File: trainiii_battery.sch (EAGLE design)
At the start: 3 parts, among them J1 B3B-XH-A(LF)(SN), J2 B3B-XH-A(LF)(SN)

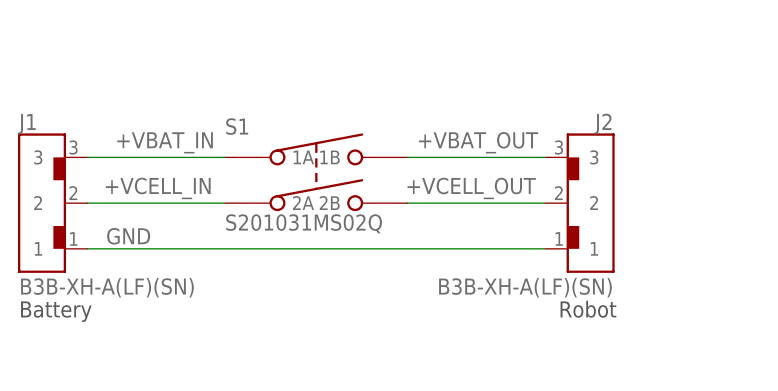
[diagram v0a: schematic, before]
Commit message: Added status LED, cleaned up board layout
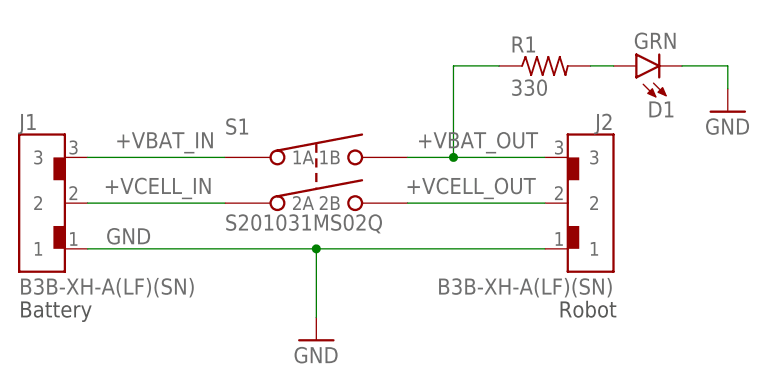
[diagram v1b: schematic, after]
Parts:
- added D1: GRN, SparkFun-LED:LED0603
- added R1: 330, rcl:R-US_R0603
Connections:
- new net LED_IN: D1.A, R1.2
- net +VBAT_OUT: now also R1.1
- net GND: now also D1.C

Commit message: Final Order v1.0
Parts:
- R1: value 330 -> 510
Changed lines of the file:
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@@
 <part name="S1" library="Trainiii Battery" deviceset="S201031MS02Q" device=""/>
 <part name="J2" library="Trainiii Battery" deviceset="B3B-XH-A(LF)(SN)" device=""/>
-<part name="R1" library="rcl" library_urn="urn:adsk.eagle:library:334" deviceset="R-US_" device="R0603" package3d_urn="urn:adsk.eagle:package:23555/3" value="330"/>
+<part name="R1" library="rcl" library_urn="urn:adsk.eagle:library:334" deviceset="R-US_" device="R0603" package3d_urn="urn:adsk.eagle:package:23555/3" value="510"/>
 <part name="GND1" library="supply1" library_urn="urn:adsk.eagle:library:371" deviceset="GND" device=""/>
 <part name="GND2" library="supply1" library_urn="urn:adsk.eagle:library:371" deviceset="GND" device=""/>
@@
 <sheet>
 <plain>
-<text x="38.1" y="50.8" size="1.778" layer="97">Battery</text>
-<text x="98.044" y="50.8" size="1.778" layer="97">Robot</text>
+<text x="38.1" y="50.8" size="1.778" layer="97" font="vector">Battery</text>
+<text x="98.044" y="50.8" size="1.778" layer="97" font="vector">Robot</text>
 </plain>
 <instances>
 <instance part="J1" gate="G$1" x="40.64" y="63.5" smashed="yes">
-<attribute name="NAME" x="38.1" y="71.628" size="1.778" layer="95"/>
-<attribute name="VALUE" x="38.1" y="53.34" size="1.778" layer="96"/>
+<attribute name="NAME" x="38.1" y="71.628" size="1.778" layer="95" font="vector"/>
+<attribute name="VALUE" x="38.1" y="53.34" size="1.778" layer="96" font="vector"/>
 </instance>
 <instance part="S1" gate="G$1" x="71.12" y="66.04" smashed="yes">
-<attribute name="NAME" x="60.96" y="71.12" size="1.778" layer="95"/>
-<attribute name="VALUE" x="60.96" y="60.452" size="1.778" layer="96"/>
+<attribute name="NAME" x="60.96" y="71.12" size="1.778" layer="95" font="vector"/>
+<attribute name="VALUE" x="60.96" y="60.452" size="1.778" layer="96" font="vector"/>
 </instance>
 <instance part="J2" gate="G$1" x="101.6" y="63.5" smashed="yes" rot="MR0">
-<attribute name="NAME" x="104.14" y="71.628" size="1.778" layer="95" rot="MR0"/>
-<attribute name="VALUE" x="104.14" y="53.34" size="1.778" layer="96" rot="MR0"/>
+<attribute name="NAME" x="104.14" y="71.628" size="1.778" layer="95" font="vector" rot="MR0"/>
+<attribute name="VALUE" x="104.14" y="53.34" size="1.778" layer="96" font="vector" rot="MR0"/>
 </instance>
 <instance part="R1" gate="G$1" x="96.52" y="78.74" smashed="yes">
-<attribute name="NAME" x="92.71" y="80.2386" size="1.778" layer="95"/>
-<attribute name="VALUE" x="92.71" y="75.438" size="1.778" layer="96"/>
+<attribute name="NAME" x="92.71" y="80.2386" size="1.778" layer="95" font="vector"/>
+<attribute name="VALUE" x="92.71" y="75.438" size="1.778" layer="96" font="vector"/>
 </instance>
 <instance part="GND1" gate="1" x="71.12" y="48.26" smashed="yes">
@@
 </instance>
 <instance part="GND2" gate="1" x="116.84" y="73.66" smashed="yes">
-<attribute name="VALUE" x="114.3" y="71.12" size="1.778" layer="96"/>
+<attribute name="VALUE" x="114.3" y="71.12" size="1.778" layer="96" font="vector"/>
 </instance>
 <instance part="D1" gate="G$1" x="106.68" y="78.74" smashed="yes" rot="R90">
-<attribute name="NAME" x="110.998" y="74.803" size="1.778" layer="95" rot="R180"/>
-<attribute name="VALUE" x="111.252" y="80.645" size="1.778" layer="96" rot="R180" align="top-left"/>
+<attribute name="NAME" x="110.998" y="74.803" size="1.778" layer="95" font="vector" rot="R180"/>
+<attribute name="VALUE" x="111.252" y="83.185" size="1.778" layer="96" font="vector" rot="R180"/>
 </instance>
 </instances>
@@
 <pinref part="J1" gate="G$1" pin="3"/>
 <wire x1="60.96" y1="68.58" x2="45.72" y2="68.58" width="0.1524" layer="91"/>
-<label x="48.768" y="69.596" size="1.778" layer="95"/>
+<label x="48.768" y="69.596" size="1.778" layer="95" font="vector"/>
 </segment>
 </net>
@@
 <pinref part="J1" gate="G$1" pin="2"/>
 <wire x1="60.96" y1="63.5" x2="45.72" y2="63.5" width="0.1524" layer="91"/>
-<label x="47.498" y="64.516" size="1.778" layer="95"/>
+<label x="47.498" y="64.516" size="1.778" layer="95" font="vector"/>
 </segment>
 </net>
@@
 <wire x1="81.28" y1="68.58" x2="86.36" y2="68.58" width="0.1524" layer="91"/>
 <pinref part="J2" gate="G$1" pin="3"/>
-<label x="82.296" y="69.596" size="1.778" layer="95"/>
+<label x="82.296" y="69.596" size="1.778" layer="95" font="vector"/>
 <wire x1="86.36" y1="68.58" x2="96.52" y2="68.58" width="0.1524" layer="91"/>
 <wire x1="86.36" y1="68.58" x2="86.36" y2="78.74" width="0.1524" layer="91"/>
@@
 <wire x1="45.72" y1="58.42" x2="71.12" y2="58.42" width="0.1524" layer="91"/>
 <pinref part="J2" gate="G$1" pin="1"/>
-<label x="47.752" y="58.928" size="1.778" layer="95"/>
+<label x="47.752" y="58.928" size="1.778" layer="95" font="vector"/>
 <wire x1="71.12" y1="58.42" x2="96.52" y2="58.42" width="0.1524" layer="91"/>
 <wire x1="71.12" y1="58.42" x2="71.12" y2="50.8" width="0.1524" layer="91"/>
@@
 <wire x1="81.28" y1="63.5" x2="96.52" y2="63.5" width="0.1524" layer="91"/>
 <pinref part="J2" gate="G$1" pin="2"/>
-<label x="81.026" y="64.516" size="1.778" layer="95"/>
+<label x="81.026" y="64.516" size="1.778" layer="95" font="vector"/>
 </segment>
 </net>
